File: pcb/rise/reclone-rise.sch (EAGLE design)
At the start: 130 parts, among them Y1 12MHz

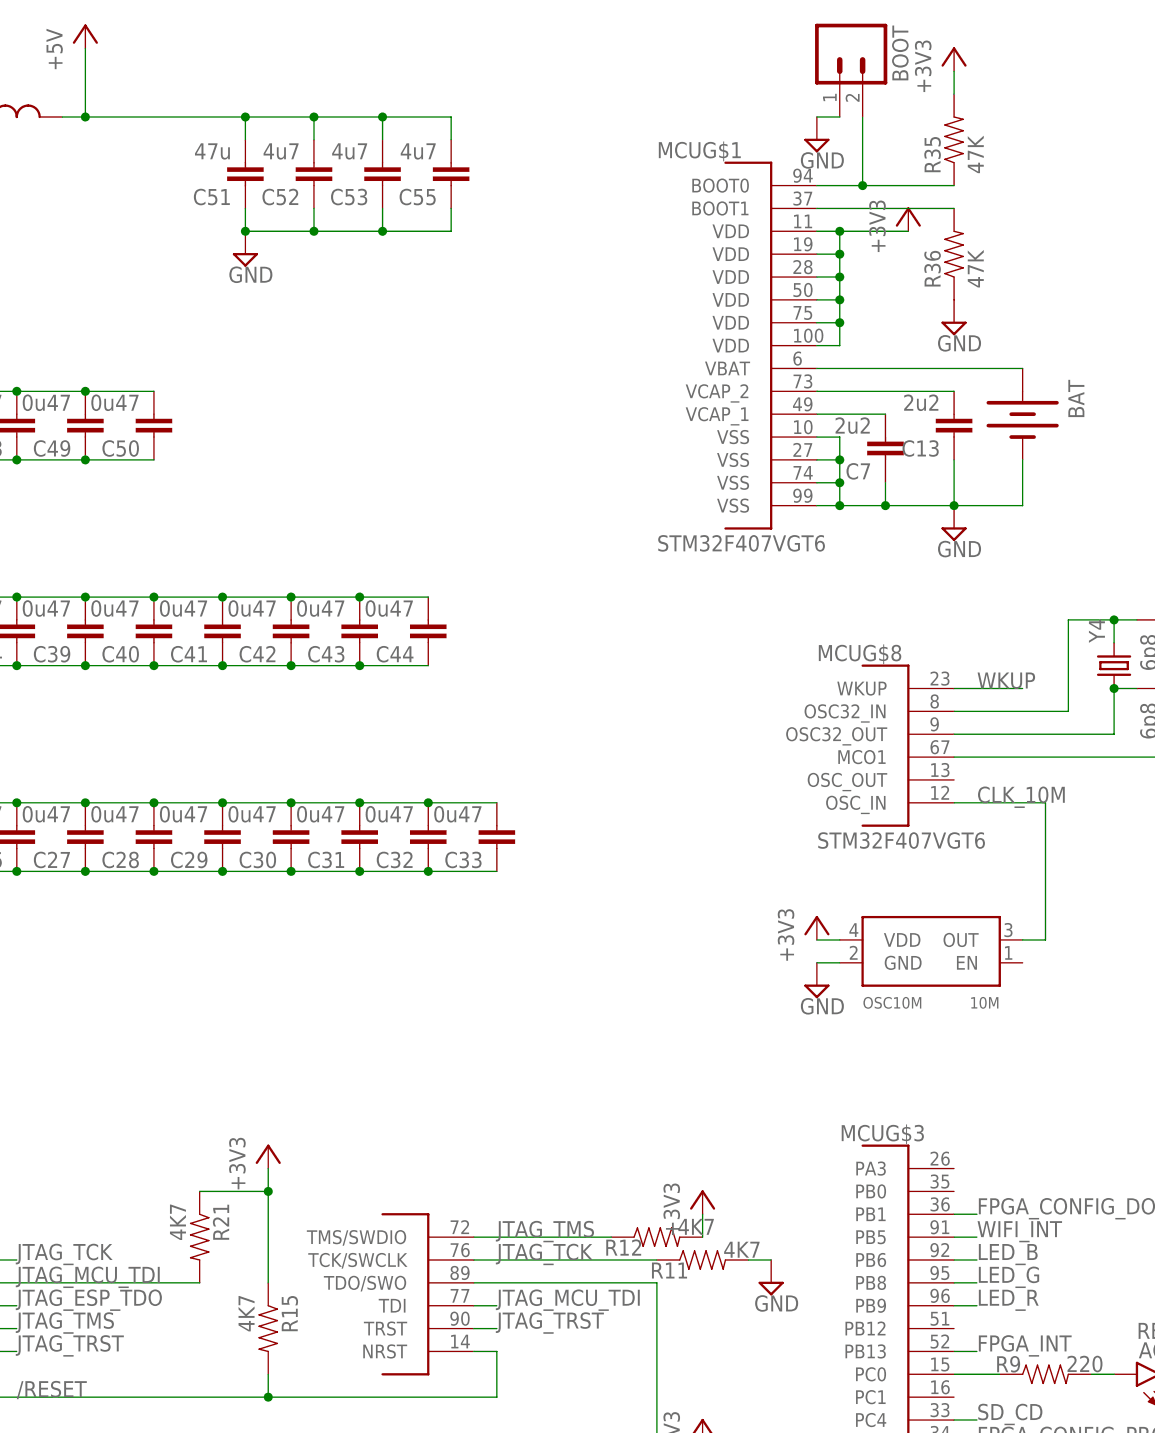
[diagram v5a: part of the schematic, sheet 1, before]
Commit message: Routed JTAG pull up/down resistors
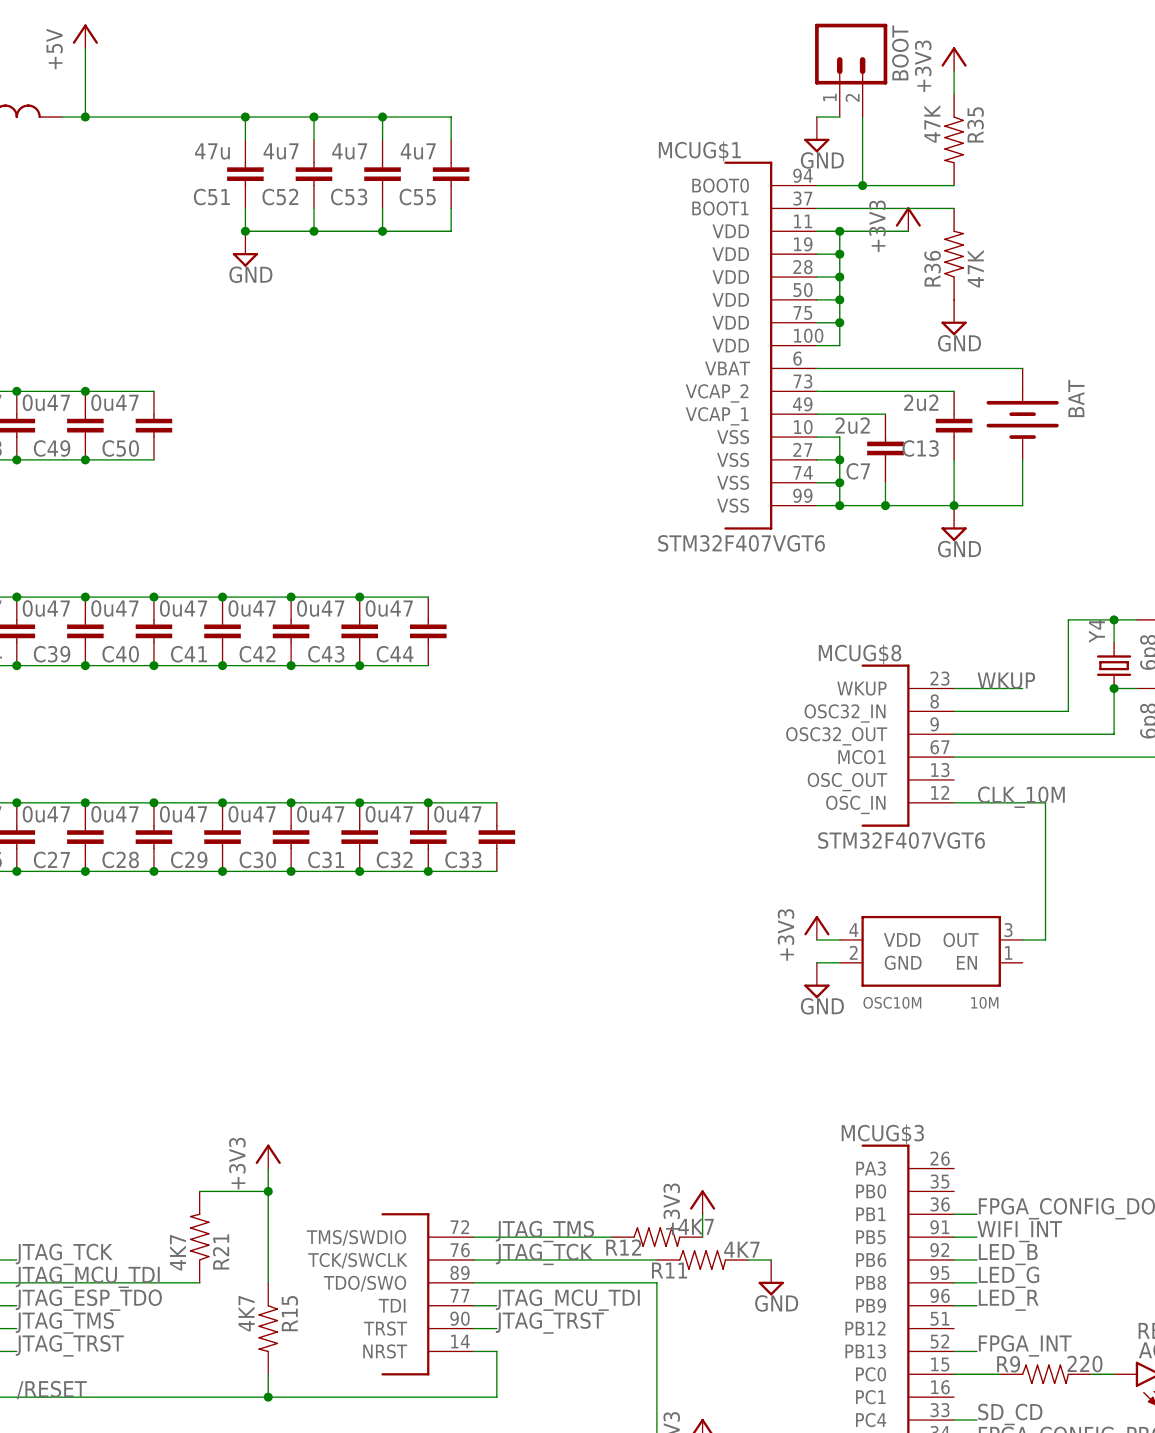
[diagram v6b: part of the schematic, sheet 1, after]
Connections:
- removed net M3A14: FPGAB3.IO_L55N_M3A14_3
- removed net M3A15: FPGAB3.IO_L83P_3
- net +3V3: now also R21.2, R35.1; no longer R21.1, R35.2
- net BOOT0: now also R35.2; no longer R35.1
- net JTAG_MCU_TDI: now also R21.1; no longer R21.2
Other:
- moved on the sheet: R21, R35
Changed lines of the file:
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@@
 <instance part="MCU" gate="G$11" x="154.94" y="50.8"/>
 <instance part="MCU" gate="G$8" x="203.2" y="157.48"/>
-<instance part="R35" gate="G$1" x="213.36" y="233.68" rot="R90"/>
+<instance part="R35" gate="G$1" x="213.36" y="233.68" rot="R270"/>
 <instance part="R36" gate="G$1" x="213.36" y="220.98" rot="R90"/>
 <instance part="+3V22" gate="G$1" x="213.36" y="243.84"/>
@@
 </instance>
 <instance part="+3V13" gate="G$1" x="185.42" y="91.44"/>
-<instance part="R21" gate="G$1" x="129.54" y="111.76" rot="R270"/>
+<instance part="R21" gate="G$1" x="129.54" y="111.76" rot="MR90"/>
 <instance part="MCU" gate="G$3" x="208.28" y="104.14"/>
 <instance part="R22" gate="G$1" x="251.46" y="226.06" rot="R270"/>
@@
 <pinref part="+3V11" gate="G$1" pin="+3V3"/>
 <wire x1="137.16" y1="106.68" x2="137.16" y2="116.84" width="0.1524" layer="91"/>
-<pinref part="R21" gate="G$1" pin="1"/>
+<pinref part="R21" gate="G$1" pin="2"/>
 <wire x1="137.16" y1="116.84" x2="137.16" y2="119.38" width="0.1524" layer="91"/>
 <wire x1="129.54" y1="116.84" x2="137.16" y2="116.84" width="0.1524" layer="91"/>
@@
 <pinref part="+3V22" gate="G$1" pin="+3V3"/>
 <wire x1="213.36" y1="238.76" x2="213.36" y2="241.3" width="0.1524" layer="91"/>
-<pinref part="R35" gate="G$1" pin="2"/>
+<pinref part="R35" gate="G$1" pin="1"/>
 </segment>
 <segment>
@@
 <pinref part="USBSER" gate="G$1" pin="ADBUS1"/>
 <label x="109.22" y="106.68" size="1.778" layer="95"/>
-<pinref part="R21" gate="G$1" pin="2"/>
+<pinref part="R21" gate="G$1" pin="1"/>
 <wire x1="106.68" y1="106.68" x2="129.54" y2="106.68" width="0.1524" layer="91"/>
 </segment>
@@
 <net name="BOOT0" class="0">
 <segment>
-<pinref part="R35" gate="G$1" pin="1"/>
+<pinref part="R35" gate="G$1" pin="2"/>
 <pinref part="MCU" gate="G$1" pin="BOOT0"/>
 <wire x1="213.36" y1="228.6" x2="203.2" y2="228.6" width="0.1524" layer="91"/>
@@
 </segment>
 </net>
-<net name="M3A14" class="0">
-<segment>
-<wire x1="271.78" y1="15.24" x2="276.86" y2="15.24" width="0.1524" layer="91"/>
-<label x="274.32" y="15.24" size="1.778" layer="95"/>
-<pinref part="FPGA" gate="B3" pin="IO_L55N_M3A14_3"/>
-</segment>
-</net>
 <net name="M3CLKN" class="0">
 <segment>
@@
 </segment>
 </net>
-<net name="M3A15" class="0">
-<segment>
-<wire x1="271.78" y1="12.7" x2="276.86" y2="12.7" width="0.1524" layer="91"/>
-<label x="274.32" y="12.7" size="1.778" layer="95"/>
-<pinref part="FPGA" gate="B3" pin="IO_L83P_3"/>
-</segment>
-</net>

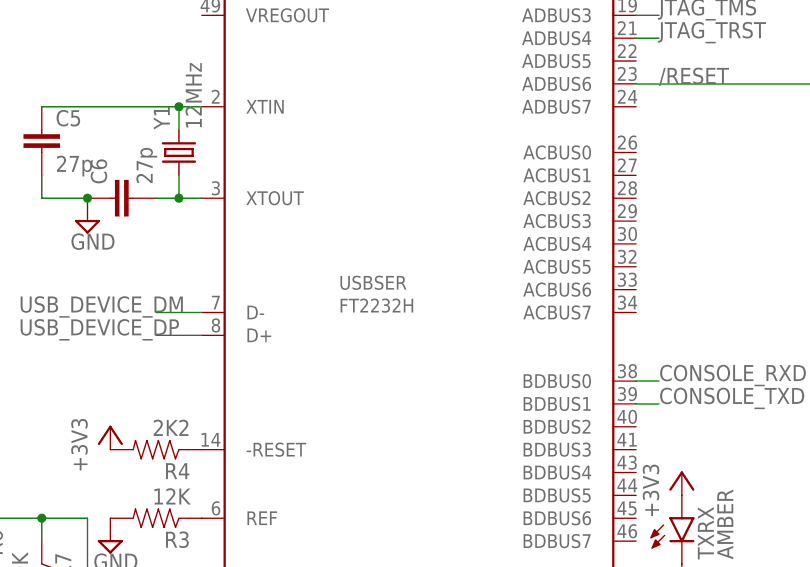
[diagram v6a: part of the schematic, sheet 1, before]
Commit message: Added meanders to match lengths on differential pairs
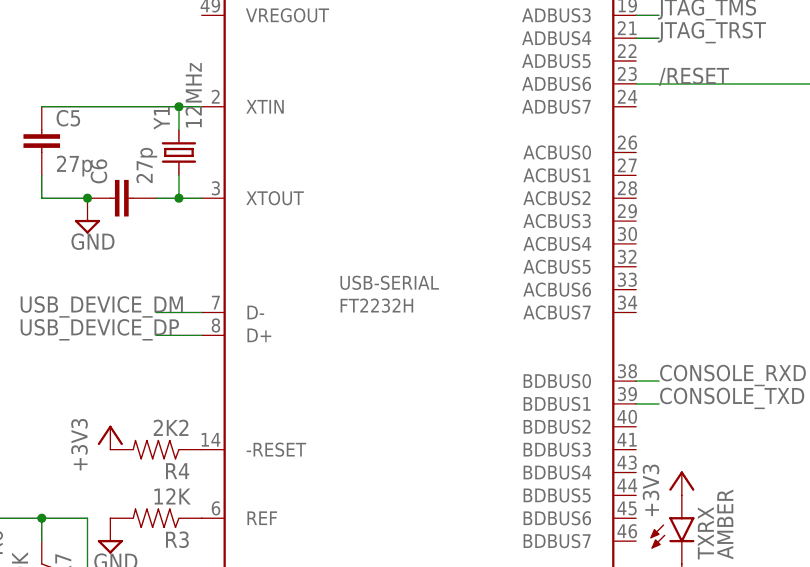
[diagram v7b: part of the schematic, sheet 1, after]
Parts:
- renumbered USBSER to USB-SERIAL
